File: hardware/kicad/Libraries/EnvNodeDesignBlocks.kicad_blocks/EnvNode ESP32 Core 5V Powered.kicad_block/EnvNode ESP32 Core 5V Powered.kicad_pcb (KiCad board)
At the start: 2 copper layers, 2 parts, among them U2 ESP32-DevKitC, U3 24AA025E-OT

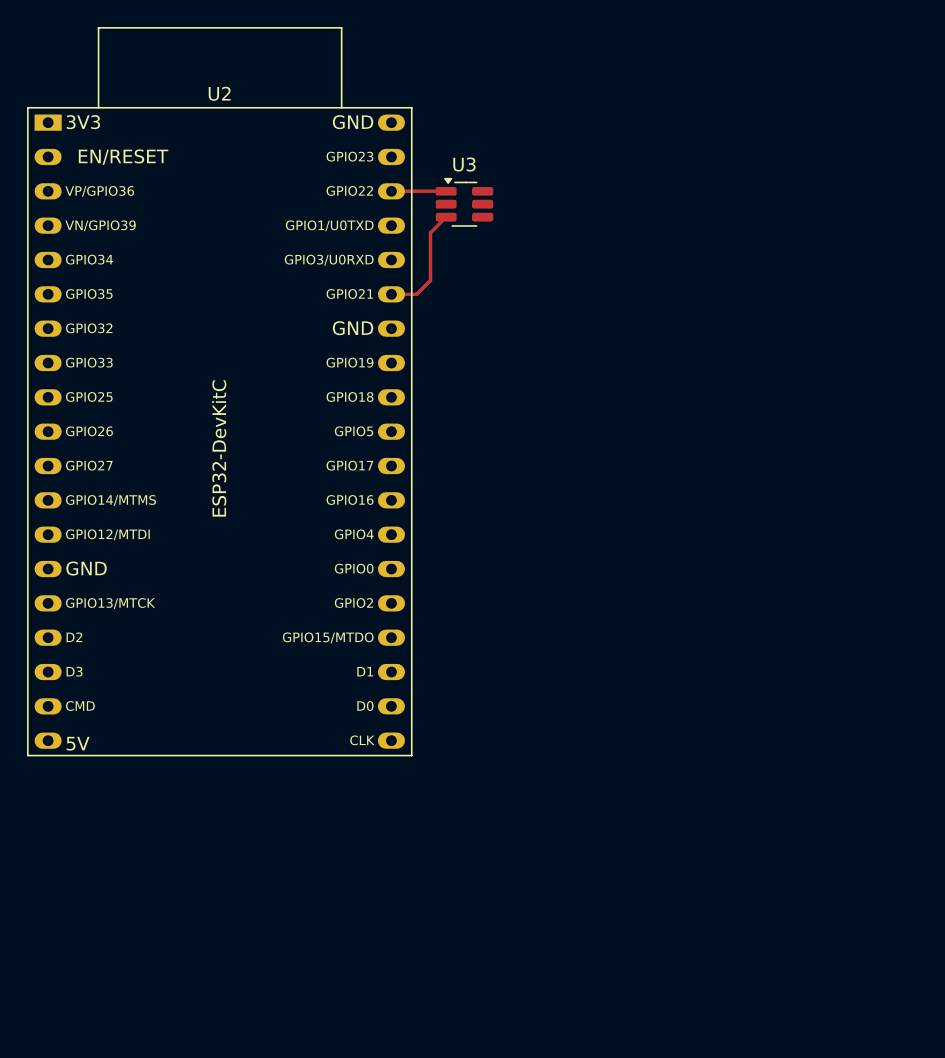
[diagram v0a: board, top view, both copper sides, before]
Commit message: DesignBlocks for ESP32 Core
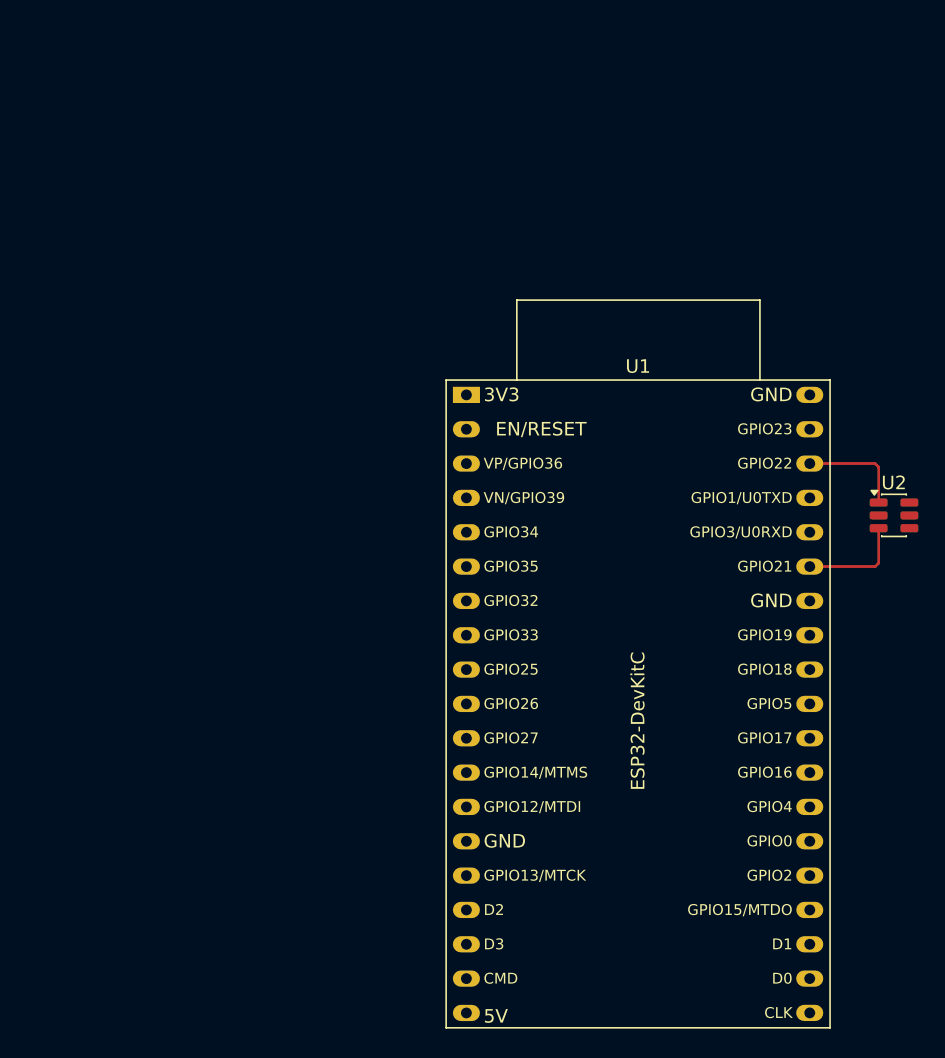
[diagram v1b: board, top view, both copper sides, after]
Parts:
- removed U3: 24AA025E-OT, Package_TO_SOT_SMD:SOT-23-6_Handsoldering
- added U1: ESP32-DevKitC, PCM_Espressif:ESP32-DevKitC, F.Cu at (146.1, 65.3)
- U2: value ESP32-DevKitC -> 24AA025E-OT; footprint PCM_Espressif:ESP32-DevKitC -> Package_TO_SOT_SMD:SOT-23-6
- moved U2 69.0 mm to (177.7, 74.2)
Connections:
- U2 pad 1: unconnected-(U2-3V3-Pad1) -> I2C0_SCL
- U2 pad 2: unconnected-(U2-CHIP_PU-Pad2) -> GND
- U2 pad 3: GPIO36 -> I2C0_SDA
- U2 pad 4: GPIO39 -> GND
- U2 pad 5: GPIO34 -> GND
- U2 pad 6: GPIO35 -> unconnected-(U2-V_{CC}-Pad6)
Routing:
- net I2C0_SCL: track 4.04 -> 7.83 mm
- net I2C0_SDA: track 8.48 -> 7.78 mm
